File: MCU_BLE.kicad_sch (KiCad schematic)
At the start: 39 parts, among them Q1 DMG1012T, U1 STM32WB55RGVx, U3 AT25SL321-U, Y1 32MHz, Y2 32.768k

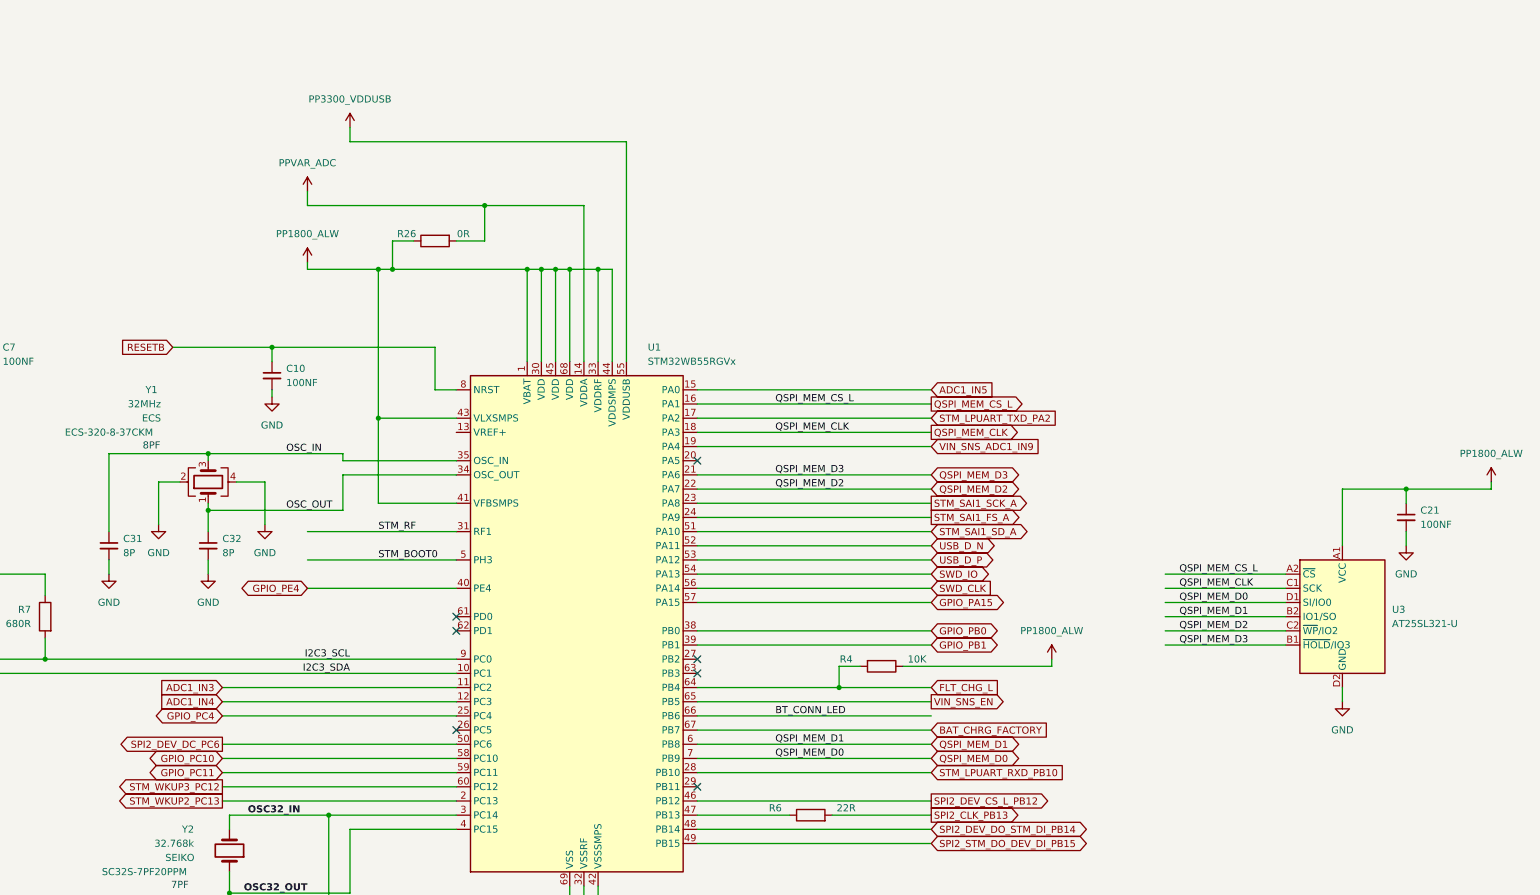
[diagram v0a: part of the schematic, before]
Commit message: Adding outputs, updated some component values.
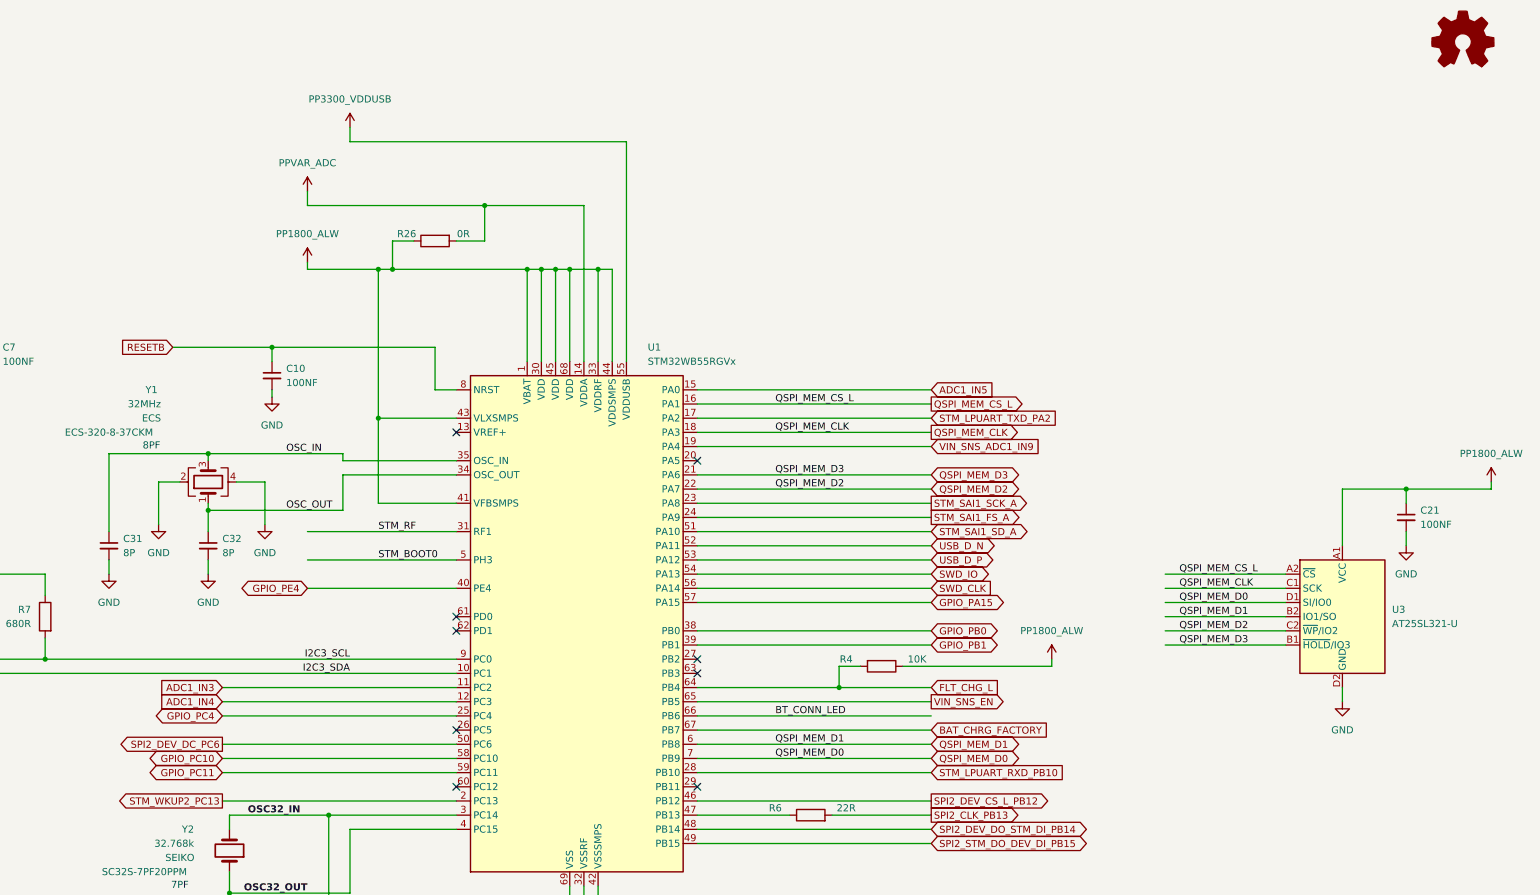
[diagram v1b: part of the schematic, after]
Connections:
- net STM_WKUP3_PC12: no longer names the net of U1.60 (PC12)
- no-connect marks 7 -> 9
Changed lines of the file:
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@@
 	)
 	(no_connect
+		(at 210.82 160.02)
+	)
+	(no_connect
+		(at 210.82 96.52)
+	)
+	(no_connect
 		(at 210.82 132.08)
 	)
@@
 	(wire
 		(pts
-			(xy 168.91 160.02) (xy 210.82 160.02)
-		)
-		(stroke
-			(width 0)
-			(type default)
-		)
-	)
-	(wire
-		(pts
 			(xy 278.13 165.1) (xy 295.91 165.1)
 		)
@@
 		)
 	)
-	(global_label "STM_WKUP3_PC12"
-		(shape output)
-		(at 168.91 160.02 180)
-		(fields_autoplaced yes)
-		(effects
-			(font
-				(size 1.27 1.27)
-			)
-			(justify right)
-		)
-		(property "Intersheetrefs" "${INTERSHEET_REFS}"
-			(at 148.8707 160.02 0)
-			(effects
-				(font
-					(size 1.27 1.27)
-				)
-				(justify right)
-				(hide yes)
-			)
-		)
-	)
 	(global_label "STM_LPUART_RXD_PB10"
 		(shape input)
@@
 					(unit 1)
 				)
+			)
+		)
+	)
+	(symbol
+		(lib_id "Graphic:Logo_Open_Hardware_Small")
+		(at 391.16 26.67 0)
+		(unit 1)
+		(exclude_from_sim no)
+		(in_bom no)
+		(on_board no)
+		(dnp no)
+		(fields_autoplaced yes)
+		(property "Reference" "#SYM1"
+			(at 391.16 19.685 0)
+			(effects
+				(font
+					(size 1.27 1.27)
+				)
+				(hide yes)
+			)
+		)
+		(property "Value" "Logo_Open_Hardware_Small"
+			(at 391.16 32.385 0)
+			(effects
+				(font
+					(size 1.27 1.27)
+				)
+				(hide yes)
+			)
+		)
+		(property "Footprint" "Symbol:OSHW-Symbol_6.7x6mm_SilkScreen"
+			(at 391.16 26.67 0)
+			(effects
+				(font
+					(size 1.27 1.27)
+				)
+				(hide yes)
+			)
+		)
+		(property "Datasheet" "~"
+			(at 391.16 26.67 0)
+			(effects
+				(font
+					(size 1.27 1.27)
+				)
+				(hide yes)
+			)
+		)
+		(property "Description" "Open Hardware logo, small"
+			(at 391.16 26.67 0)
+			(effects
+				(font
+					(size 1.27 1.27)
+				)
+				(hide yes)
+			)
+		)
+		(property "Sim.Enable" "0"
+			(at 391.16 26.67 0)
+			(effects
+				(font
+					(size 1.27 1.27)
+				)
+				(hide yes)
+			)
+		)
+		(instances
+			(project "Bluetooth_OSHW"
+				(path "/45b78866-6047-4631-b3ef-230df13ace1e/7b2dfbe2-907a-422c-96c9-24d772068968"
+					(reference "#SYM1")
+					(unit 1)
+				)

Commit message: removed backup zips. adding updated output files
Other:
- title: nRF Battery Dev Kit -> stm32_bluet_pill
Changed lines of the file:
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@@
 	(paper "A3")
 	(title_block
-		(title "nRF Battery Dev Kit")
-		(date "2024-02-26")
+		(title "stm32_bluet_pill")
+		(date "2024-04-03")
 		(rev "Proto")
 		(company "Clover Designs")
@@
 		(at 391.16 26.67 0)
 		(unit 1)
-		(exclude_from_sim no)
+		(exclude_from_sim yes)
 		(in_bom no)
 		(on_board no)
@@
 			(at 391.16 26.67 0)
 			(effects
-				(font
-					(size 1.27 1.27)
-				)
-				(hide yes)
-			)
-		)
-		(property "Sim.Enable" "0"
-			(at 391.16 26.67 0)
-			(effects

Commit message: updating design files
updating schematics, gerbers, design files, etc.
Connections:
- net SWD_O: now reaches U1.60 (PC12)
- net GPIO_PC4: no longer names the net of U1.25 (PC4)
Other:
- moved on the sheet: R26

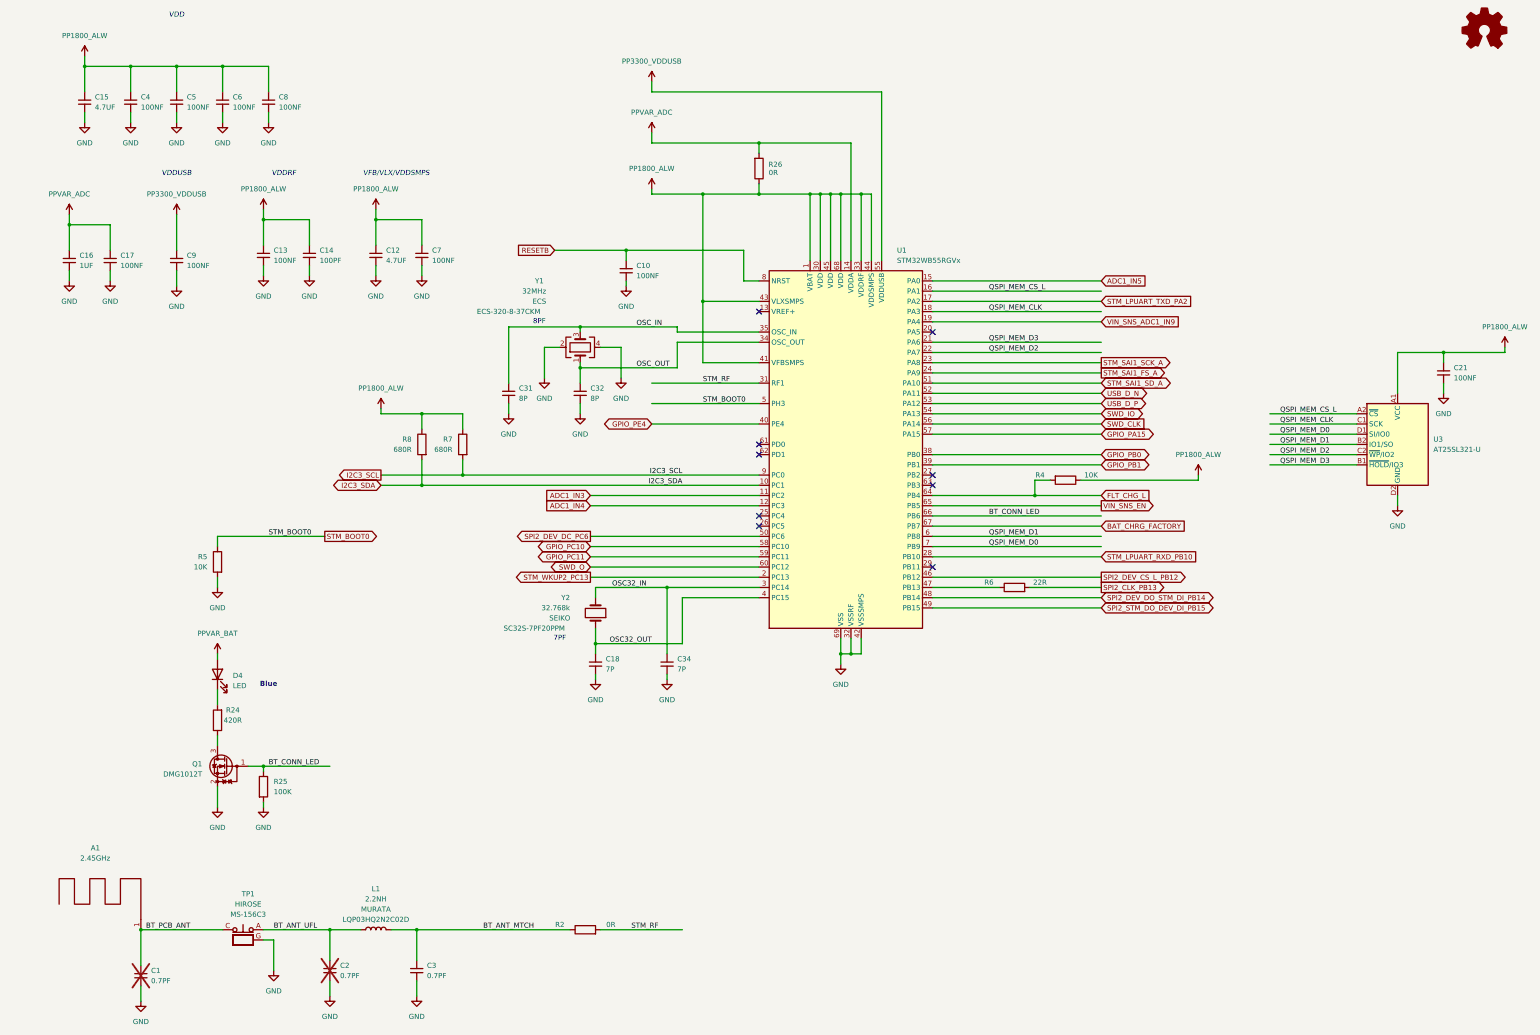
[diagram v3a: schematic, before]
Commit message: Updated project
- Changed board stackup, trace-widths
- Changed VIA size
- Fixed fab drawings
- added CHG FLT LED
- Removed unnecessary files
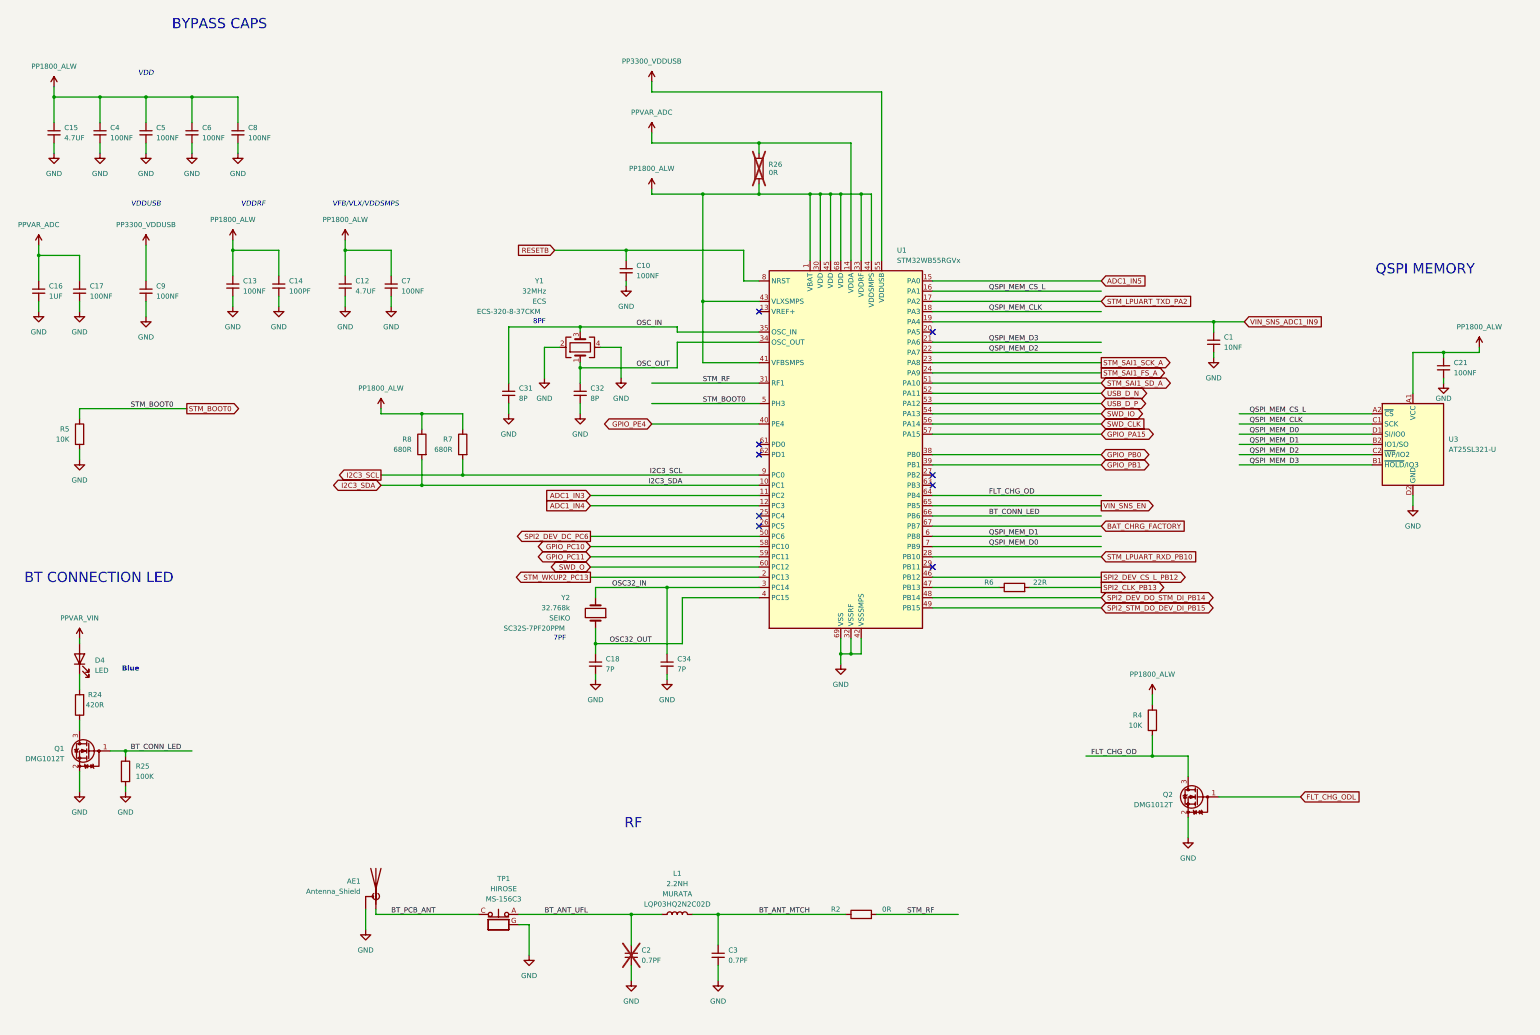
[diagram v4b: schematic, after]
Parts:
- removed A1: 2.45GHz, user_antenna:nRF52_dongle_meander_F, symbol user_antenna:nRF52_USB_DONGLE_meander_F
- added AE1: Antenna_Shield, RF_Antenna:Texas_SWRA117D_2.4GHz_Right, symbol Device:Antenna_Shield
- added Q2: DMG1012T, Package_TO_SOT_SMD:SOT-523, symbol Transistor_FET:DMG1012T
- C1: value 0.7PF -> 10NF; now fitted
- R26: now not fitted
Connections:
- net BT_PCB_ANT: now also AE1.1 (A); no longer C1.1
- net GND: now also AE1.2 (Shield), Q2.2 (S)
- net VIN_SNS_ADC1_IN9: now also C1.1
- net FLT_CHG_L renamed FLT_CHG_OD
- net FLT_CHG_OD: now also Q2.3 (D)
- net PPVAR_BAT renamed PPVAR_VIN
- new net FLT_CHG_ODL: Q2.1 (G)
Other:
- note added: "BT CONNECTION LED"
- note added: "BYPASS CAPS"
- note added: "QSPI MEMORY"
- note added: "RF"
- company: Clover Designs -> Brendan Bleker
- moved on the sheet: C12, C13, C14, C15, C16, C17, C2, C21, C3, C4, C5, C6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
